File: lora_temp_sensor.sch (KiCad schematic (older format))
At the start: 20 parts

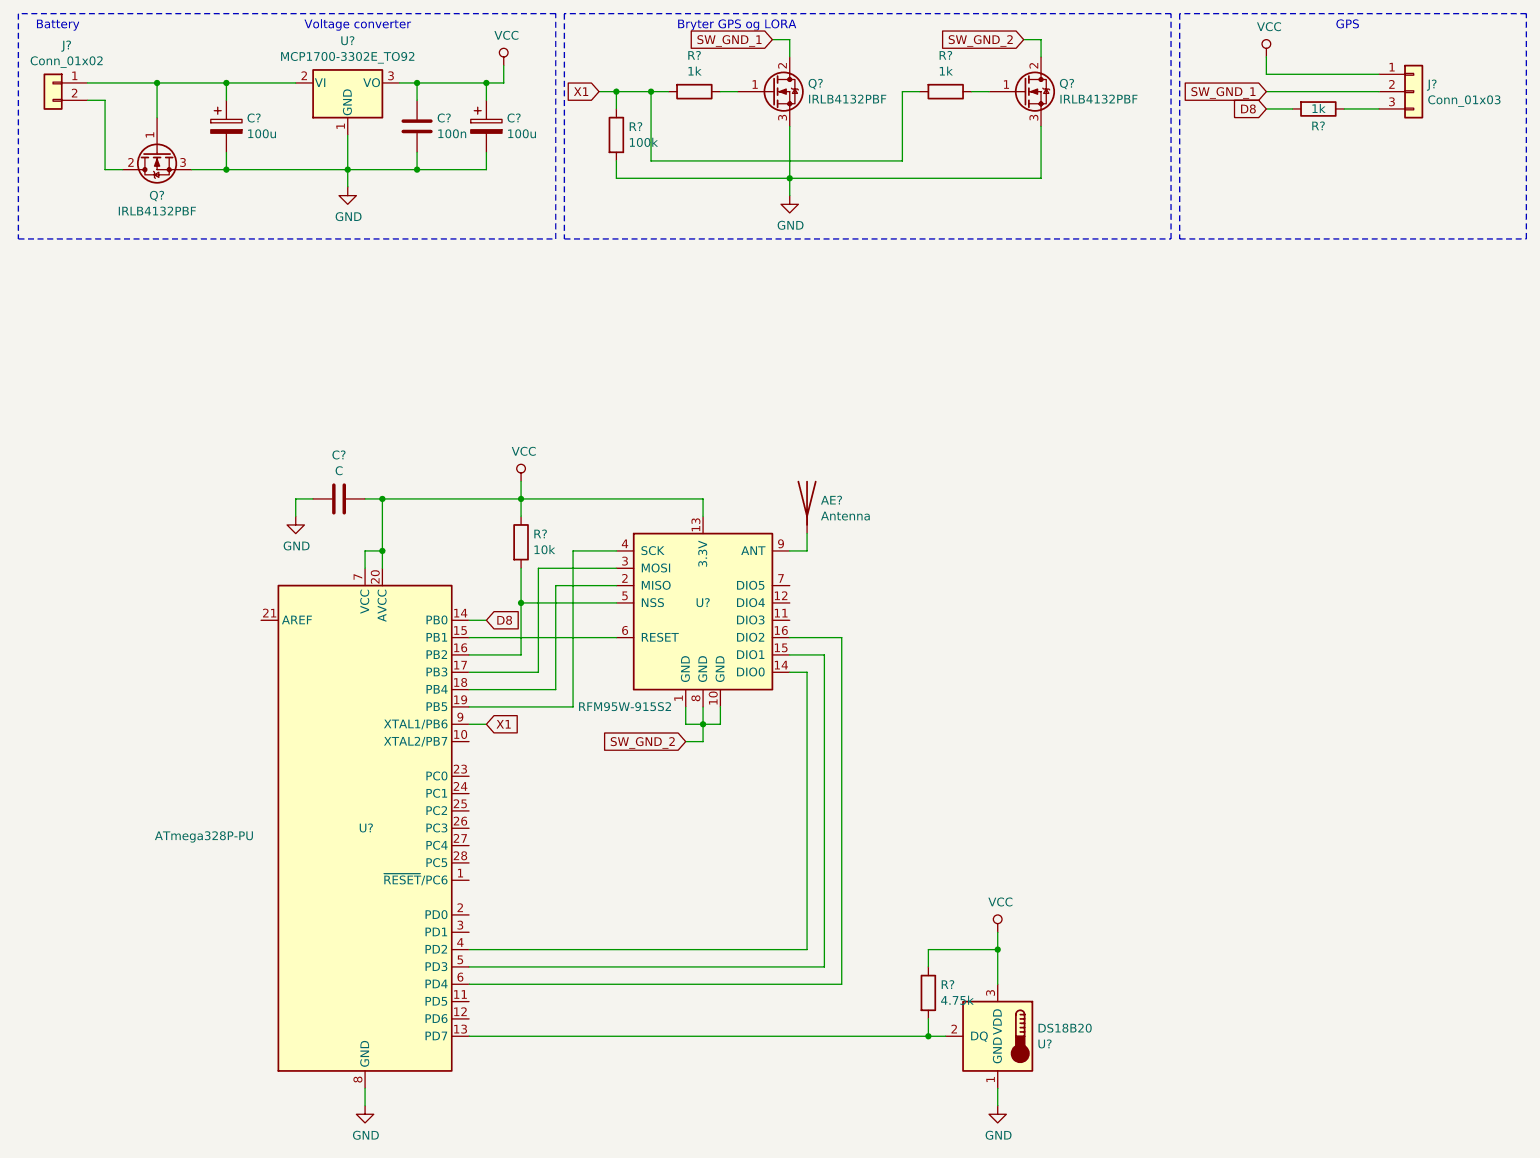
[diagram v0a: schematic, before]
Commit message: Go overboard with bypass caps for prototype
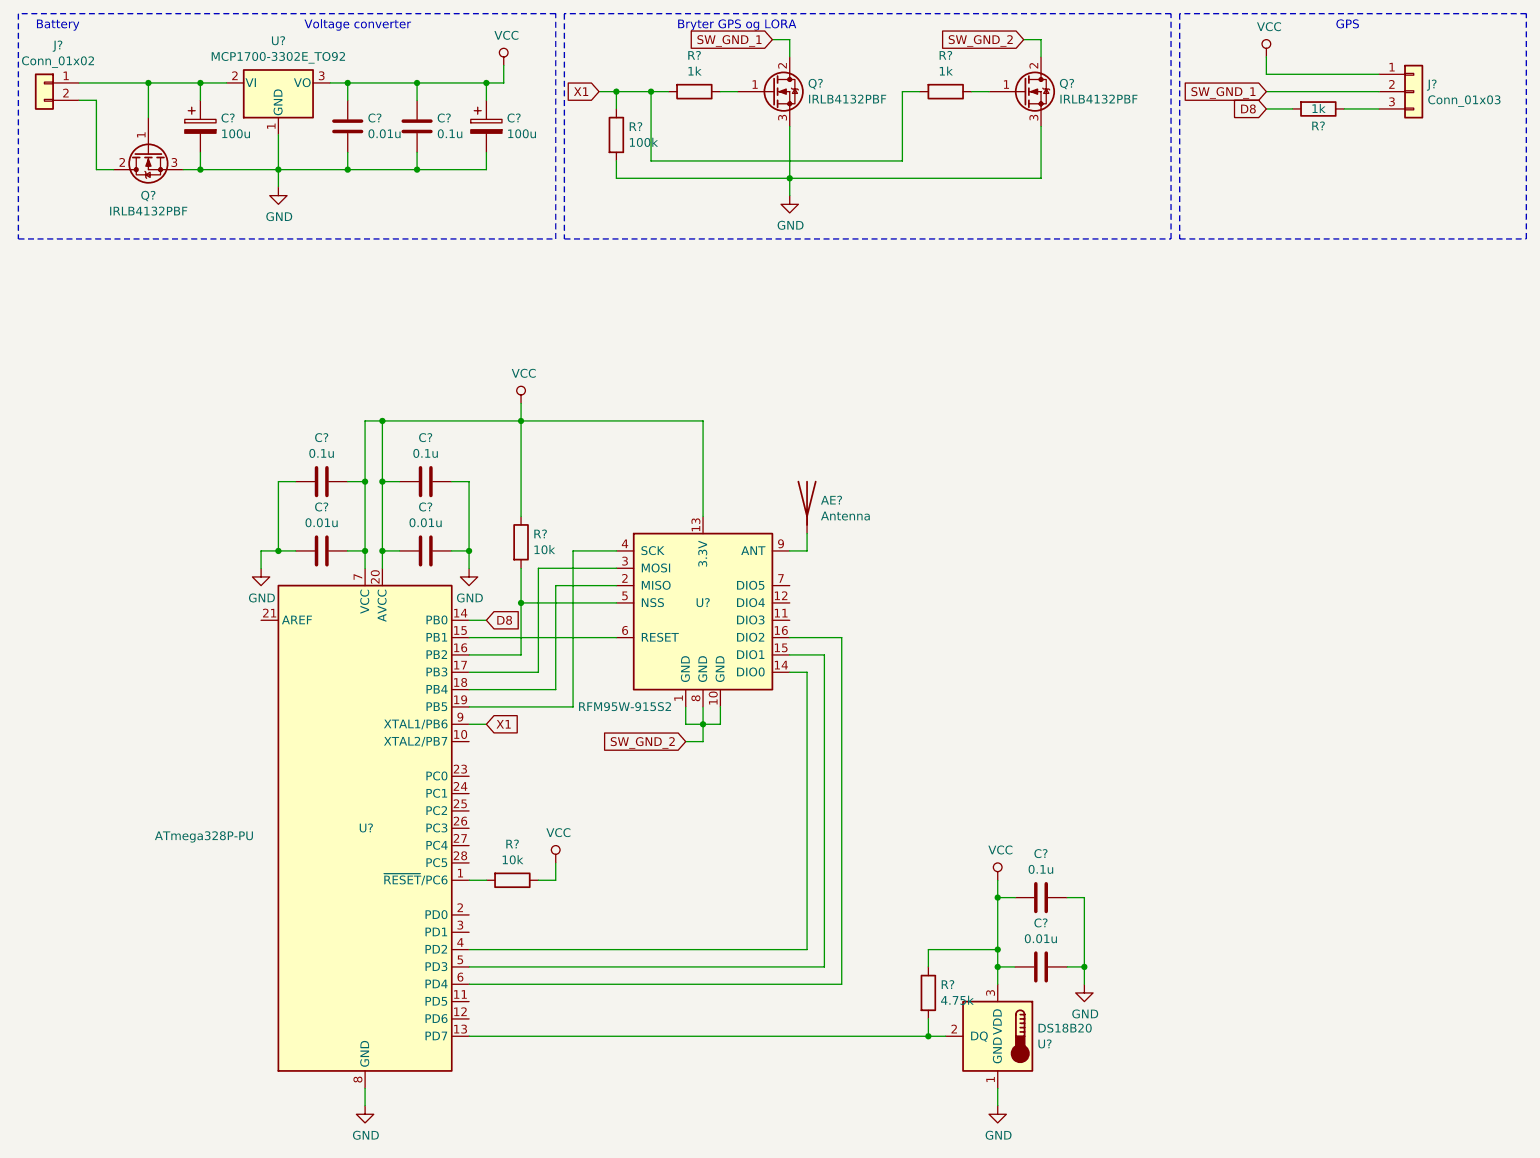
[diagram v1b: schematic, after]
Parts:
- added C? (x4): 0.01u, symbol Device:C
- added C? (x2): 0.1u, symbol Device:C
- added R?: 10k, symbol Device:R
- C?: value 100n -> 0.1u
- C?: value C -> 0.1u
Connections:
- net GND: now also C?.1, C?.1, C?.1, C?.1, C?.2, C?.2
- net VCC: now also C?.1, C?.1, C?.2, C?.2, C?.2, C?.2, R?.1
- net at U?.1 (~RESET~/PC6): now also R?.2
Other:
- moved on the sheet: C?, J?, Q?, U?

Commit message: Oppdatert tegninger og dokumentasjon
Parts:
- removed Q? (x2): IRLB4132PBF, symbol Device:Q_NMOS_GDS
- removed R? (x2): 1k, symbol Device:R
- removed R?: 100k, symbol Device:R
- added C?: 0.1u, symbol Device:C
- added Q?: IPB80P03P4L, symbol Device:Q_PMOS_GDS
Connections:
- net SW_GND_2 is gone; now on net SW_GND: U?.1 (GND), U?.10 (GND), U?.8 (GND)
- net GND: now also C?.2
- net VCC: now also C?.1, Q?.3 (S)
- net X1: now also Q?.1 (G)
- net SW_GND_1 renamed SW_GND
- new net SW_VCC: Q?.2 (D)
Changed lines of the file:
@@
 EESchema Schematic File Version 4
 LIBS:lora_temp_sensor-cache
-EELAYER 26 0
+EELAYER 29 0
 EELAYER END
 $Descr A4 11693 8268
@@
 $Comp
 L Device:Q_NMOS_GDS Q?
-U 1 1 5C617904
-P 4850 950
-F 0 "Q?" H 5055 996 50  0000 L CNN
-F 1 "IRLB4132PBF" H 5055 905 50  0000 L CNN
-F 2 "" H 5050 1050 50  0001 C CNN
-F 3 "~" H 4850 950 50  0001 C CNN
-	1    4850 950
-	1    0    0    -1
-$EndComp
-$Comp
-L Device:Q_NMOS_GDS Q?
 U 1 1 5C617994
 P 1250 1300
@@
 Text Notes 2150 600  0    50   ~ 0
 Voltage converter
-$Comp
-L Device:Q_NMOS_GDS Q?
-U 1 1 5C619A1D
-P 6300 950
-F 0 "Q?" H 6505 996 50  0000 L CNN
-F 1 "IRLB4132PBF" H 6505 905 50  0000 L CNN
-F 2 "" H 6500 1050 50  0001 C CNN
-F 3 "~" H 6300 950 50  0001 C CNN
-	1    6300 950
-	1    0    0    -1
-$EndComp
 Wire Notes Line
 	3600 1800 3600 500
@@
 Wire Notes Line
 	500  1800 3600 1800
-Text GLabel 3850 950  0    50   Input ~ 0
-X1
-$Comp
-L power:GND #PWR?
-U 1 1 5C61ADB1
-P 4950 1550
-F 0 "#PWR?" H 4950 1300 50  0001 C CNN
-F 1 "GND" H 4955 1377 50  0000 C CNN
-F 2 "" H 4950 1550 50  0001 C CNN
-F 3 "" H 4950 1550 50  0001 C CNN
-	1    4950 1550
-	1    0    0    -1
-$EndComp
-Text GLabel 4850 650  0    50   Input ~ 0
-SW_GND_1
-Text GLabel 6300 650  0    50   Input ~ 0
-SW_GND_2
-Text Notes 4300 600  0    50   ~ 0
-Bryter GPS og LORA
 Wire Notes Line
 	3650 500  3650 1800
 Wire Notes Line
-	3650 1800 7150 1800
-Wire Notes Line
 	7150 1800 7150 500
 Wire Notes Line
 	7150 500  3650 500
-$Comp
-L Device:R R?
-U 1 1 5C61CCEF
-P 4400 950
-F 0 "R?" V 4193 950 50  0000 C CNN
-F 1 "1k" V 4284 950 50  0000 C CNN
-F 2 "" V 4330 950 50  0001 C CNN
-F 3 "~" H 4400 950 50  0001 C CNN
-	1    4400 950
-	0    1    1    0
-$EndComp
-$Comp
-L Device:R R?
-U 1 1 5C61CD7D
-P 5850 950
-F 0 "R?" V 5643 950 50  0000 C CNN
-F 1 "1k" V 5734 950 50  0000 C CNN
-F 2 "" V 5780 950 50  0001 C CNN
-F 3 "~" H 5850 950 50  0001 C CNN
-	1    5850 950
-	0    1    1    0
-$EndComp
-$Comp
-L Device:R R?
-U 1 1 5C61CDF5
-P 3950 1200
-F 0 "R?" H 4020 1246 50  0000 L CNN
-F 1 "100k" H 4020 1155 50  0000 L CNN
-F 2 "" V 3880 1200 50  0001 C CNN
-F 3 "~" H 3950 1200 50  0001 C CNN
-	1    3950 1200
-	1    0    0    -1
-$EndComp
-Wire Wire Line
-	3850 950  3950 950
-Wire Wire Line
-	3950 950  3950 1050
-Connection ~ 3950 950
-Wire Wire Line
-	3950 950  4150 950
-Wire Wire Line
-	4150 950  4250 950
-Connection ~ 4150 950
-Wire Wire Line
-	4550 950  4650 950
-Wire Wire Line
-	4950 750  4950 650
-Wire Wire Line
-	4950 650  4850 650
-Wire Wire Line
-	4150 950  4150 1350
-Wire Wire Line
-	4950 1150 4950 1450
-Wire Wire Line
-	4950 1450 3950 1450
-Wire Wire Line
-	3950 1450 3950 1350
-Connection ~ 4950 1450
-Wire Wire Line
-	5700 950  5600 950
-Wire Wire Line
-	5600 950  5600 1350
-Wire Wire Line
-	4150 1350 5600 1350
-Wire Wire Line
-	6000 950  6100 950
-Wire Wire Line
-	6400 750  6400 650
-Wire Wire Line
-	6400 650  6300 650
-Wire Wire Line
-	6400 1150 6400 1450
-Wire Wire Line
-	6400 1450 4950 1450
-Wire Wire Line
-	4950 1550 4950 1450
 $Comp
 L Connector_Generic:Conn_01x03 J?
@@
 $EndComp
 Text GLabel 7700 950  0    50   Input ~ 0
-SW_GND_1
+SW_GND
 Text GLabel 7700 1050 0    50   Input ~ 0
 D8
@@
 	3100 4100 3950 4100
 Text GLabel 4350 4700 0    50   Input ~ 0
-SW_GND_2
+SW_GND
 Wire Wire Line
 	4350 4500 4350 4600
@@
 $EndComp
 Wire Wire Line
-	4450 3400 4450 2850
+	4450 3400 4450 3150
 $Comp
 L Device:R R?
@@
 	1    0    0    -1
 $EndComp
+$Comp
+L power:GND #PWR?
+U 1 1 5C870FD1
+P 3950 3250
+F 0 "#PWR?" H 3950 3000 50  0001 C CNN
+F 1 "GND" H 3955 3077 50  0000 C CNN
+F 2 "" H 3950 3250 50  0001 C CNN
+F 3 "" H 3950 3250 50  0001 C CNN
+	1    3950 3250
+	1    0    0    -1
+$EndComp
+$Comp
+L Device:C C?
+U 1 1 5C871053
+P 4200 3150
+F 0 "C?" V 3948 3150 50  0000 C CNN
+F 1 "0.1u" V 4039 3150 50  0000 C CNN
+F 2 "" H 4238 3000 50  0001 C CNN
+F 3 "~" H 4200 3150 50  0001 C CNN
+	1    4200 3150
+	0    1    1    0
+$EndComp
+Wire Wire Line
+	3950 3250 3950 3150
+Wire Wire Line
+	3950 3150 4050 3150
+Wire Wire Line
+	4350 3150 4450 3150
+Connection ~ 4450 3150
+Wire Wire Line
+	4450 3150 4450 2850
+$Comp
+L Device:Q_PMOS_GDS Q?
+U 1 1 5C8AFD8B
+P 4600 1200
+F 0 "Q?" H 4805 1154 50  0000 L CNN
+F 1 "IPB80P03P4L" H 4805 1245 50  0000 L CNN
+F 2 "" H 4800 1300 50  0001 C CNN
+F 3 "~" H 4600 1200 50  0001 C CNN
+	1    4600 1200
+	1    0    0    1
+$EndComp
+$Comp
+L power:VCC #PWR?
+U 1 1 5C8AFEC5
+P 4700 900
+F 0 "#PWR?" H 4700 750 50  0001 C CNN
+F 1 "VCC" H 4717 1073 50  0000 C CNN
+F 2 "" H 4700 900 50  0001 C CNN
+F 3 "" H 4700 900 50  0001 C CNN
+	1    4700 900
+	1    0    0    -1
+$EndComp
+Wire Wire Line
+	4700 900  4700 1000
+Wire Wire Line
+	4700 1400 4700 1500
+Wire Wire Line
+	4700 1500 4600 1500
+Wire Wire Line
+	4400 1200 4300 1200
+Text GLabel 4300 1200 0    50   Input ~ 0
+X1
+Text GLabel 4600 1500 0    50   Input ~ 0
+SW_VCC
+Wire Notes Line
+	3650 1800 7150 1800
+Text Notes 4300 600  0    50   ~ 0
+Bryter GPS og LORA
 $EndSCHEMATC

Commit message: Update schematics and documentation
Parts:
- U?: symbol RF_AM_FM:RFM95W-915S2 -> lora_temp_sensor-rescue:RFM95W-915S2-RF_AM_FM
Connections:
- net SW_GND is gone; now on net GND: J?.2 (Pin_2), U?.1 (GND), U?.10 (GND), U?.8 (GND)
- net SW_VCC: now also C?.1, C?.2, C?.2, J?.1 (Pin_1), R?.1, U?.13 (3.3V), U?.3 (VDD)
- net VCC: no longer C?.1, C?.2, C?.2, J?.1 (Pin_1), R?.1, U?.13 (3.3V), U?.3 (VDD)
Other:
- moved on the sheet: R?
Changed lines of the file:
@@
 Connection ~ 3200 900
 $Comp
-L RF_AM_FM:RFM95W-915S2 U?
+L lora_temp_sensor-rescue:RFM95W-915S2-RF_AM_FM U?
 U 1 1 5C6192AD
 P 4450 3900
@@
 	1    0    0    -1
 $EndComp
-$Comp
-L power:VCC #PWR?
-U 1 1 5C62898B
-P 7700 750
-F 0 "#PWR?" H 7700 600 50  0001 C CNN
-F 1 "VCC" H 7717 923 50  0000 C CNN
-F 2 "" H 7700 750 50  0001 C CNN
-F 3 "" H 7700 750 50  0001 C CNN
-	1    7700 750
-	1    0    0    -1
-$EndComp
-Text GLabel 7700 950  0    50   Input ~ 0
-SW_GND
-Text GLabel 7700 1050 0    50   Input ~ 0
+Text GLabel 7850 1050 0    50   Input ~ 0
 D8
 Text Notes 8100 600  0    50   ~ 0
@@
 L Device:R R?
 U 1 1 5C628BE6
-P 8000 1050
-F 0 "R?" V 8100 1050 50  0000 C CNN
-F 1 "1k" V 8000 1050 50  0000 C CNN
-F 2 "" V 7930 1050 50  0001 C CNN
-F 3 "~" H 8000 1050 50  0001 C CNN
-	1    8000 1050
-	0    1    1    0
-$EndComp
-Wire Wire Line
-	7700 750  7700 850
-Wire Wire Line
-	7700 850  8350 850
-Wire Wire Line
-	7700 950  8350 950
-Wire Wire Line
-	8350 1050 8150 1050
-Wire Wire Line
-	7850 1050 7700 1050
+P 8100 1050
+F 0 "R?" V 8200 1050 50  0000 C CNN
+F 1 "1k" V 8100 1050 50  0000 C CNN
+F 2 "" V 8030 1050 50  0001 C CNN
+F 3 "~" H 8100 1050 50  0001 C CNN
+	1    8100 1050
+	0    1    1    0
+$EndComp
+Wire Wire Line
+	8350 1050 8250 1050
+Wire Wire Line
+	7950 1050 7850 1050
 Wire Notes Line
 	7200 500  7200 1800
@@
 Wire Wire Line
 	3100 4100 3950 4100
-Text GLabel 4350 4700 0    50   Input ~ 0
-SW_GND
 Wire Wire Line
 	4350 4500 4350 4600
@@
 Wire Wire Line
 	4450 4600 4450 4700
-Wire Wire Line
-	4450 4700 4350 4700
 $Comp
 L power:VCC #PWR?
@@
 Wire Wire Line
 	3400 3400 3400 2850
-Wire Wire Line
-	3400 2850 4450 2850
 Wire Wire Line
 	3400 2850 3400 2750
@@
 Wire Wire Line
 	5750 5900 5750 6000
-$Comp
-L power:VCC #PWR?
-U 1 1 5C764849
-P 6150 5500
-F 0 "#PWR?" H 6150 5350 50  0001 C CNN
-F 1 "VCC" H 6167 5673 50  0000 C CNN
-F 2 "" H 6150 5500 50  0001 C CNN
-F 3 "" H 6150 5500 50  0001 C CNN
-	1    6150 5500
-	1    0    0    -1
-$EndComp
 Connection ~ 6150 5900
 Connection ~ 5750 6400
@@
 Wire Wire Line
 	4350 3150 4450 3150
-Connection ~ 4450 3150
-Wire Wire Line
-	4450 3150 4450 2850
 $Comp
 L Device:Q_PMOS_GDS Q?
@@
 Text Notes 4300 600  0    50   ~ 0
 Bryter GPS og LORA
+Text GLabel 4350 2700 0    50   Input ~ 0
+SW_VCC
+Wire Wire Line
+	4350 2700 4450 2700
+Wire Wire Line
+	4450 2700 4450 3150
+Connection ~ 4450 3150
+$Comp
+L power:GND #PWR?
+U 1 1 5CF0DDC1
+P 4450 4700
+F 0 "#PWR?" H 4450 4450 50  0001 C CNN
+F 1 "GND" H 4455 4527 50  0000 C CNN
+F 2 "" H 4450 4700 50  0001 C CNN
+F 3 "" H 4450 4700 50  0001 C CNN
+	1    4450 4700
+	1    0    0    -1
+$EndComp
+Text GLabel 8250 850  0    50   Input ~ 0
+SW_VCC
+Wire Wire Line
+	8250 850  8350 850
+$Comp
+L power:GND #PWR?
+U 1 1 5CF1D3FF
+P 7550 1050
+F 0 "#PWR?" H 7550 800 50  0001 C CNN
+F 1 "GND" H 7555 877 50  0000 C CNN
+F 2 "" H 7550 1050 50  0001 C CNN
+F 3 "" H 7550 1050 50  0001 C CNN
+	1    7550 1050
+	1    0    0    -1
+$EndComp
+Wire Wire Line
+	7550 1050 7550 950
+Wire Wire Line
+	7550 950  8350 950
+Text GLabel 6050 5500 0    50   Input ~ 0
+SW_VCC
+Wire Wire Line
+	6050 5500 6150 5500
 $EndSCHEMATC
